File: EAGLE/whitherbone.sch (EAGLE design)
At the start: 219 parts, among them IC1 A4983, IC12 TPS2051BDGN, IC13 SN74AUC1G74, IC14 TPD4S012DRY, IC15 TPD4S012DRY, IC17 SN74LVC2G241DCUR, IC2 SN74LVC1G07DCK, IC4 7805T, IC7 IP4283CZ10-TBR, IC8 IP4283CZ10-TBR, IC9 TDA19988BHN/C1,557, J1 1-1747981-1, Q2 32.768kHz, Q4 24 MHz, T1 BSS138W-7-F, T3 BSS138W-7-F, T4 BSS138W-7-F, U1 OSD3358-512M-BSM, U2 SN74AHCT125PW, X2 SCHA5B0200, X4 10118192-0001LF

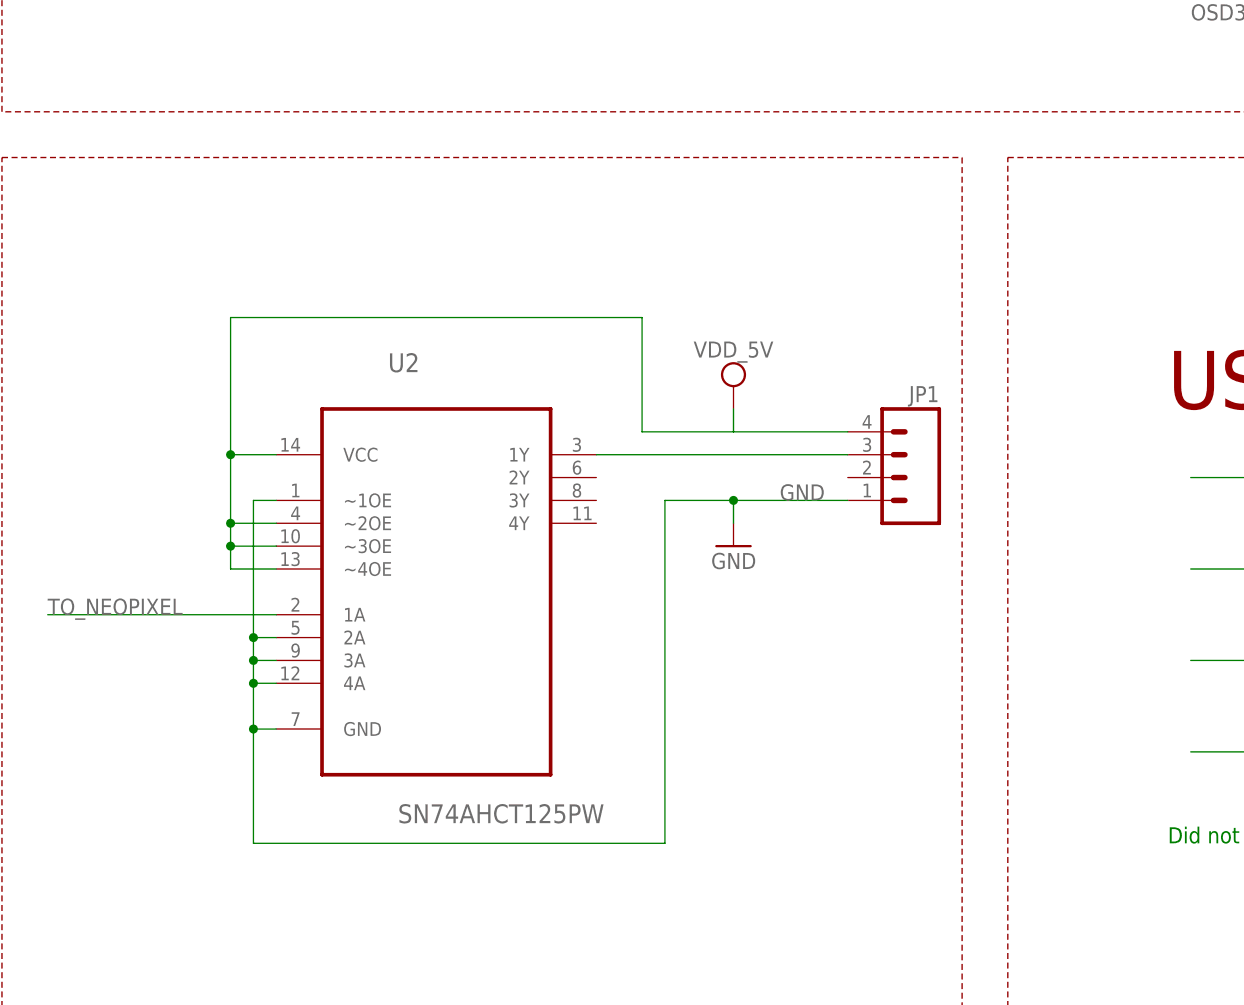
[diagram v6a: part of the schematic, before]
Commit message: Add quick decoupling cap for neopixel output
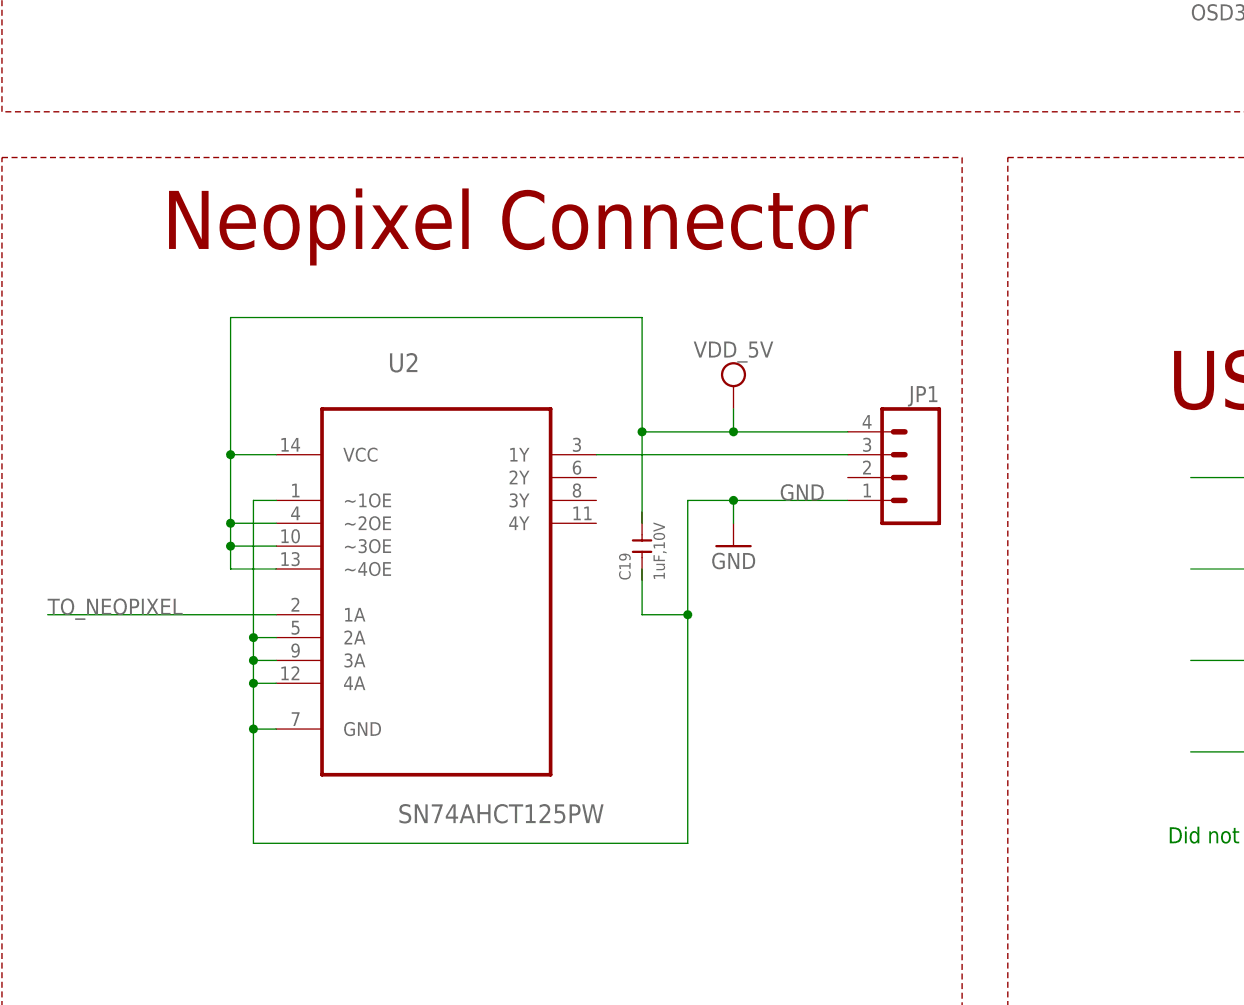
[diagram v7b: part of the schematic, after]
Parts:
- added C19: 1uF,10V, Seeed-Capacitor:CERAMIC-1UF-10V-10%-X5R(0402)
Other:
- note added: "Neopixel Connector"
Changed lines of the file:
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@@
 <part name="SUPPLY10" library="GHI-PowerGoundSupply" deviceset="VDD_5V" device=""/>
 <part name="U2" library="SN74AHCT125PW" deviceset="SN74AHCT125PW" device=""/>
+<part name="C19" library="Seeed-Capacitor" deviceset="CERAMIC-1UF-10V-10%-X5R(0402)" device="" value="1uF,10V"/>
 </parts>
 <sheets>
@@
 <text x="541.02" y="7.62" size="1.778" layer="98">Attribution 3.0 US License</text>
 <text x="548.386" y="20.32" size="1.778" layer="98">Motor current 0mA to over 2A/phase</text>
+<text x="652.78" y="144.78" size="6.4516" layer="94" ratio="10">Neopixel Connector</text>
 </plain>
 <instances>
@@
 <instance part="SUPPLY10" gate="G$1" x="716.28" y="129.54" rot="MR0"/>
 <instance part="U2" gate="A" x="683.26" y="109.22"/>
+<instance part="C19" gate="G$1" x="706.12" y="111.76" rot="R90"/>
 </instances>
 <busses>
@@
 <pinref part="GND27" gate="1" pin="GND"/>
 <wire x1="716.28" y1="116.84" x2="716.28" y2="114.3" width="0.1524" layer="91"/>
-<wire x1="716.28" y1="116.84" x2="708.66" y2="116.84" width="0.1524" layer="91"/>
+<wire x1="716.28" y1="116.84" x2="711.2" y2="116.84" width="0.1524" layer="91"/>
 <junction x="716.28" y="116.84"/>
 <pinref part="U2" gate="A" pin="GND"/>
 <wire x1="665.48" y1="91.44" x2="662.94" y2="91.44" width="0.1524" layer="91"/>
 <wire x1="662.94" y1="91.44" x2="662.94" y2="78.74" width="0.1524" layer="91"/>
-<wire x1="662.94" y1="78.74" x2="708.66" y2="78.74" width="0.1524" layer="91"/>
-<wire x1="708.66" y1="78.74" x2="708.66" y2="116.84" width="0.1524" layer="91"/>
+<wire x1="662.94" y1="78.74" x2="711.2" y2="78.74" width="0.1524" layer="91"/>
+<wire x1="711.2" y1="78.74" x2="711.2" y2="104.14" width="0.1524" layer="91"/>
 <pinref part="U2" gate="A" pin="~1OE"/>
+<wire x1="711.2" y1="104.14" x2="711.2" y2="116.84" width="0.1524" layer="91"/>
 <wire x1="665.48" y1="116.84" x2="662.94" y2="116.84" width="0.1524" layer="91"/>
 <wire x1="662.94" y1="116.84" x2="662.94" y2="101.6" width="0.1524" layer="91"/>
@@
 <junction x="662.94" y="99.06"/>
 <junction x="662.94" y="101.6"/>
+<wire x1="706.12" y1="104.14" x2="711.2" y2="104.14" width="0.1524" layer="91"/>
+<wire x1="706.12" y1="104.14" x2="706.12" y2="109.22" width="0.1524" layer="91"/>
+<junction x="711.2" y="104.14"/>
 </segment>
 </net>
@@
 <junction x="660.4" y="111.76"/>
 <junction x="660.4" y="121.92"/>
+<junction x="716.28" y="124.46"/>
+<wire x1="706.12" y1="124.46" x2="706.12" y2="114.3" width="0.1524" layer="91"/>
+<junction x="706.12" y="124.46"/>
 </segment>
 </net>
